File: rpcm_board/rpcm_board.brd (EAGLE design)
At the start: 72 x 56 mm, 57 parts, among them Q4 DMG1012T, U1 SFW15R-1STE1LF, U2 SFW15R-1STE1LF, U3 DMG1012T, U4 MICROSD_SD_MODEMOLEX, U5 PAM2306DYPAA

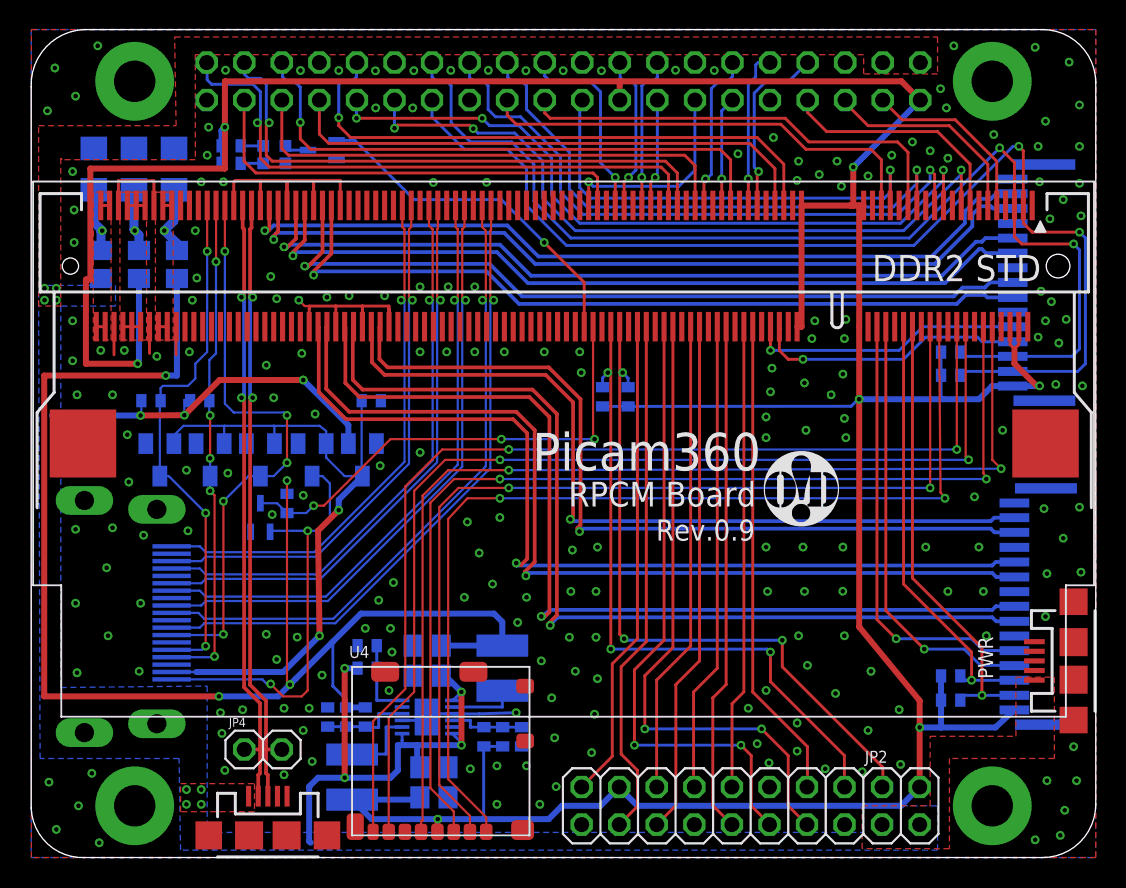
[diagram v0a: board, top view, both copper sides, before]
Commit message: camera_unit, camera_adapter
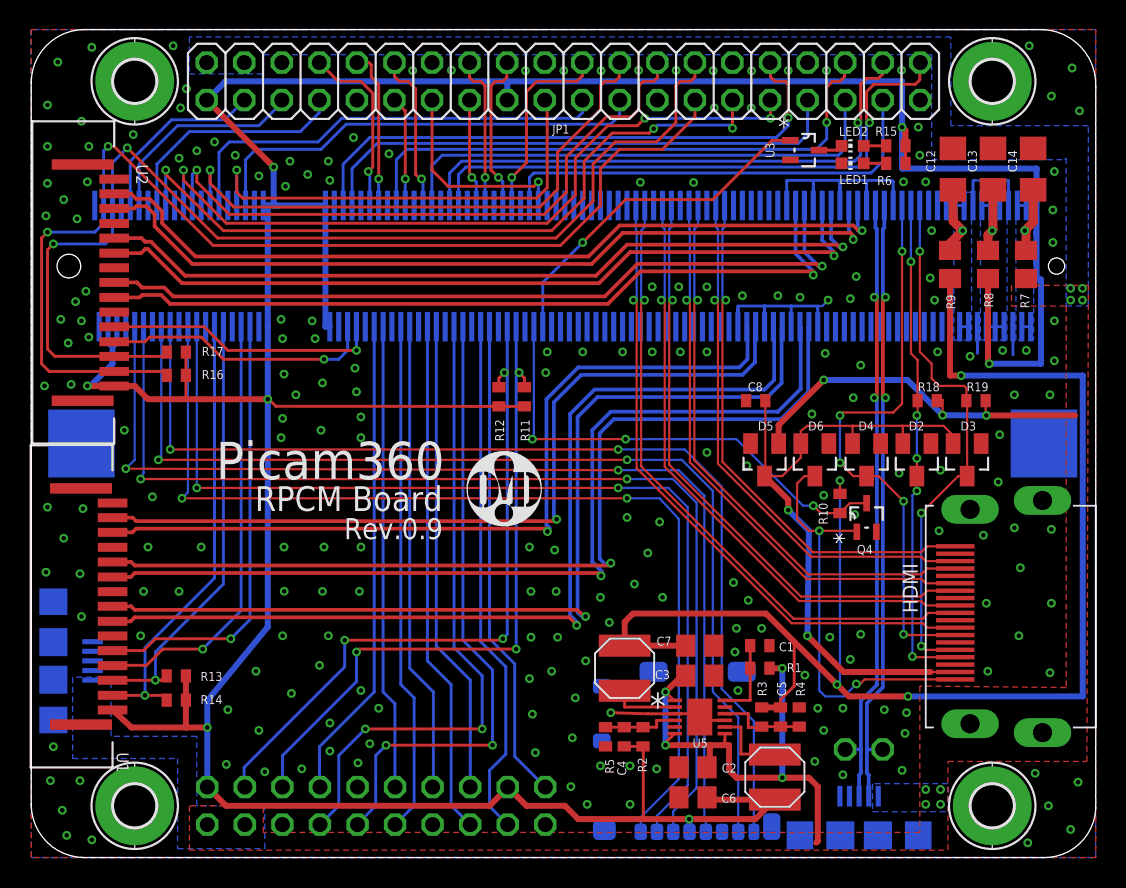
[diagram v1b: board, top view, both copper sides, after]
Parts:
- moved JP3 69.0 mm to (1.50, 13.3), flipped to the bottom
- moved C14 63.5 mm to (67.8, 46.6), flipped to the top
- moved R7 62.6 mm to (67.3, 40.1), flipped to the top
- moved HDMI 61.0 mm to (66.5, 16.3), flipped to the top
- moved C13 58.1 mm to (65.0, 46.6), flipped to the top
- moved H1 58.0 mm to (65.0, 52.5), flipped to the top
- moved H2 58.0 mm to (7.00, 52.5), flipped to the top
- moved H3 58.0 mm to (7.00, 3.50), flipped to the top
- moved H4 58.0 mm to (65.0, 3.50), flipped to the top
- moved R8 57.4 mm to (64.7, 40.1), flipped to the top
- moved R19 55.8 mm to (63.9, 30.9), flipped to the top
- moved U1 55.5 mm to (8.25, 17.0), flipped to the top
- moved U2 55.3 mm to (8.36, 38.9), flipped to the top
- moved D3 54.6 mm to (63.3, 26.9), flipped to the top
- moved C12 52.7 mm to (62.3, 46.6), flipped to the top
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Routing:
- added copper zone on layer 16, net CM_1V8
- added copper zone on layer 16, net CM_3V3
- added copper zone on layer 16, net CM_VBAT
- removed copper zone on layer 1, net CM_1V8
- removed copper zone on layer 1, net CM_3V3
- removed copper zone on layer 1, net CM_VBAT
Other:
- outline, holes or cut-outs redrawn

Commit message: interface board 0.7 rpcm board 0.10
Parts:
- removed JP4: (no value), openblw:1X02
- added C11: 4.7n, resistor:C0402
- added R20: 1M, resistor:R0402
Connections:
- new net USB2_SHELL: C11.1, JP6.MT1, JP6.MT2, JP6.P$1, JP6.P$2, R20.1
- net GND: now also C11.2, R20.2
- net USB_D_N: no longer JP4.1
- net USB_D_P: no longer JP4.2
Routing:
- net +3V3: track 255.1 -> 37.6 mm, vias 7 -> 18
- net +1V8: track 97.4 -> 57.9 mm
- net +5V: track 60.8 -> 62.4 mm, vias 15 -> 12
- net USB_D_P: track 42.3 -> 41.2 mm
- net USB_D_N: track 42.3 -> 41.2 mm
- net CAM1_IO1: track 18.5 -> 19.5 mm
- net CAM1_IO0: track 18.7 -> 19.3 mm
- net GND: track 57.2 -> 56.6 mm, vias 217 -> 155
- added copper zone on layer 2, net +3V3
- added copper zone on layer 2, net +5V
- added copper zone on layer 15, net GND
- added copper zone on layer 1, net USB2_SHELL
- added copper zone on layer 16, net USB2_SHELL
- removed copper zone on layer 1, net +5V
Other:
- board text added: "Rev.0.10"
- board text removed: "Rev.0.9"

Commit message: tune value
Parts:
- R10: value 100k -> 100K
- R18, R19: value 1k8 -> 1.8K
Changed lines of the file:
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@@
 <?xml version="1.0" encoding="utf-8"?>
 <!DOCTYPE eagle SYSTEM "eagle.dtd">
-<eagle version="8.1.1">
+<eagle version="8.4.2">
 <drawing>
 <settings>
 <setting alwaysvectorfont="no"/>
+<setting keepoldvectorfont="yes"/>
 <setting verticaltext="up"/>
 </settings>
@@
 <param name="dpMaxLengthDifference" value="10mm"/>
 <param name="dpGapFactor" value="2.5"/>
-<param name="checkGrid" value="0"/>
 <param name="checkAngle" value="0"/>
 <param name="checkFont" value="1"/>
 <param name="checkRestrict" value="0"/>
+<param name="checkStop" value="0"/>
 <param name="useDiameter" value="13"/>
 <param name="maxErrors" value="50"/>
@@
 <attribute name="VALUE" x="54.905" y="30.075" size="0.6096" layer="27" rot="R180" display="off"/>
 </element>
-<element name="R10" library="resistor" package="R0402" value="100k" x="54.7" y="23.95" smashed="yes" rot="R90">
+<element name="R10" library="resistor" package="R0402" value="100K" x="54.7" y="23.95" smashed="yes" rot="R90">
 <attribute name="NAME" x="53.865" y="22.515" size="0.6096" layer="25" rot="R90"/>
 <attribute name="VALUE" x="56.605" y="23.315" size="0.6096" layer="27" rot="R90" display="off"/>
@@
 <attribute name="VALUE" x="60.945" y="19.5456" size="0.6096" layer="27" ratio="10" rot="SR90" display="off"/>
 </element>
-<element name="R18" library="resistor" package="R0402" value="1k8" x="60.6" y="30.9" smashed="yes">
+<element name="R18" library="resistor" package="R0402" value="1.8K" x="60.6" y="30.9" smashed="yes">
 <attribute name="NAME" x="59.965" y="31.535" size="0.6096" layer="25"/>
 <attribute name="VALUE" x="59.965" y="28.995" size="1.27" layer="27" display="off"/>
 </element>
-<element name="R19" library="resistor" package="R0402" value="1k8" x="63.9" y="30.9" smashed="yes">
+<element name="R19" library="resistor" package="R0402" value="1.8K" x="63.9" y="30.9" smashed="yes">
 <attribute name="NAME" x="63.265" y="31.535" size="0.6096" layer="25"/>
 <attribute name="VALUE" x="63.265" y="28.995" size="1.27" layer="27" display="off"/>
